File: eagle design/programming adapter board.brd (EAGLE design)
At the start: 24.1 x 14 mm, 2 parts

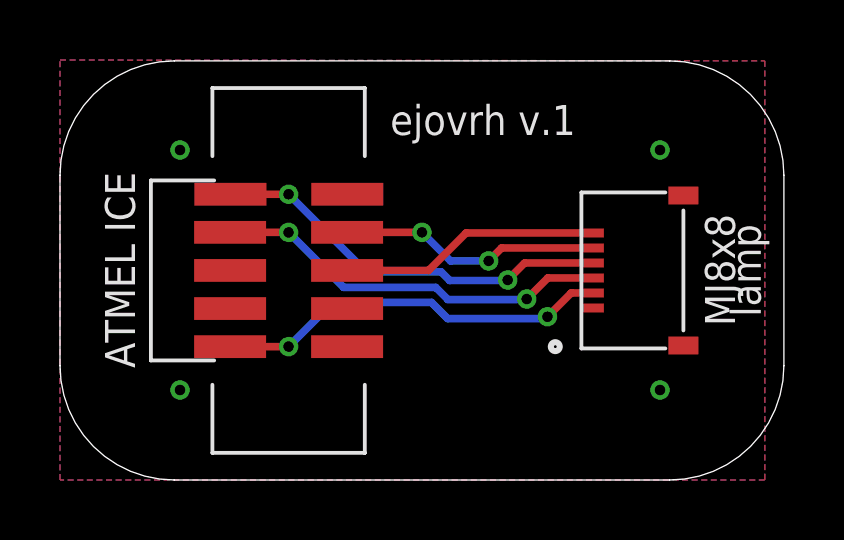
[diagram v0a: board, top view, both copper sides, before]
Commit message: - consolidated eagle libraries into one folder - updated programming board and created gerber files
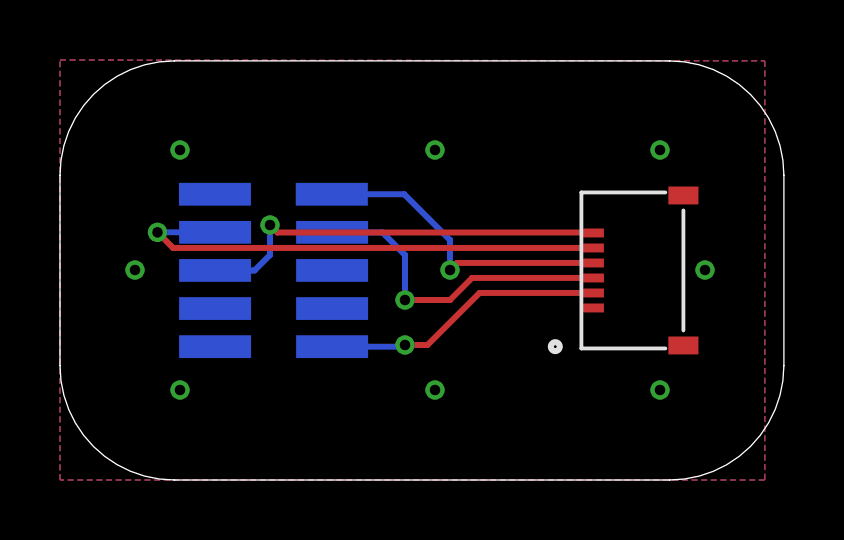
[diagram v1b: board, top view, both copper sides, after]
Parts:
- moved ATMEL_ICE 0.50 mm to (7.12, 6.99), flipped to the bottom
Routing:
- net 5V0: track 8.78 -> 16.7 mm, vias 2 -> 1
- net DEBUGWIRE/RESET: track 8.73 -> 13.9 mm, vias 0 -> 1
- net ICSP_MOSI: track 13.3 -> 9.45 mm, vias 2 -> 1
- net ICSP_SCK: track 13.5 -> 10.4 mm, vias 2 -> 1
- net ICSP_MISO: track 13.3 -> 10.8 mm, vias 2 -> 1
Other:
- board text added: "ejovrh v.2"
- board text removed: "MJ8x8"
- board text removed: "ejovrh v.1"
